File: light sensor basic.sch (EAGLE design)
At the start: 1 part

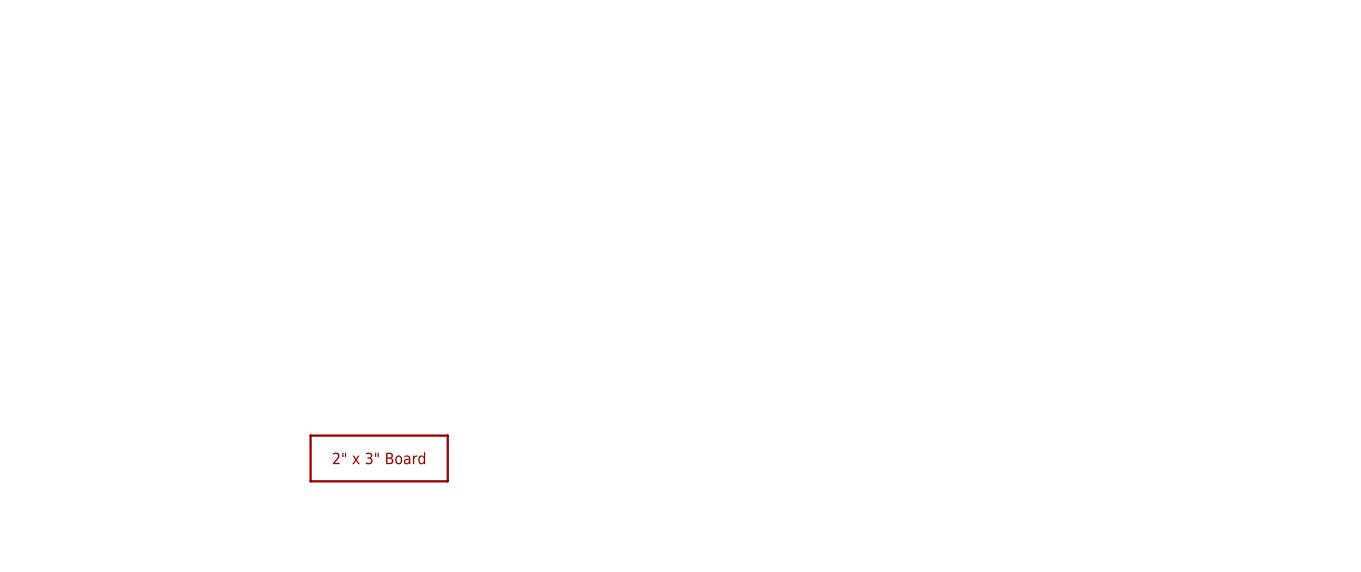
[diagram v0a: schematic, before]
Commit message: Update light sensor basic.sch
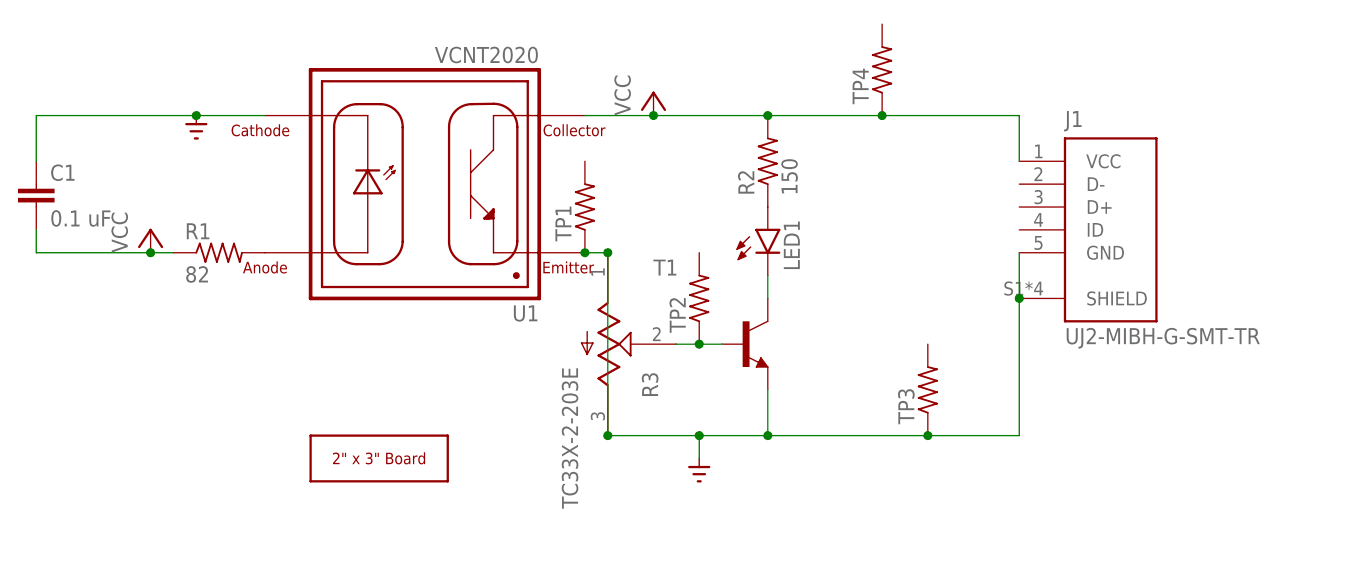
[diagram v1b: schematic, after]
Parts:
- added C1: 0.1 uF, rcl:C-EUC1206
- added J1: UJ2-MIBH-G-SMT-TR, UJ2-MIBH-G-SMT-TR:UJ2-MIBH-G-SMT-TR
- added LED1: (no value), led:LEDSML0805
- added R1: 82, rcl:R-US_R0805
- added R2: 150, rcl:R-US_R0805
- added R3: TC33X-2-203E, TC33X-2-203E:TC33X-2-203E
- added T1: (no value), transistor:-NPN-SOT23-EBC
- added TP1, TP2, TP3, TP4: (no value), rcl:R-US_R1206
- added U1: VCNT2020, VCNT2020:VCNT2020
- U$1: value 2X3_BOARD_V2 -> 2X3_BOARD; device voltera_community_lib:2X3_BOARD_V2 -> voltera_community_lib:2X3_BOARD
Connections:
- new net GND: C1.1, J1.GND, J1.SHIELD, R3.CCW, R3.CW, T1.E, TP1.1, TP3.1, U1.CATHODE, U1.EMITTER
- new net N$1: R1.2, U1.ANODE
- new net N$2: J1.VCC, R2.2, TP4.1, U1.COLLECTOR
- new net N$4: R3.W, T1.B, TP2.1
- new net N$5: LED1.C, T1.C
- new net N$6: LED1.A, R2.1
- new net VCC: C1.2, R1.1

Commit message: Update board
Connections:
- removed net N$2: J1.VCC, R2.2, TP4.1, U1.COLLECTOR
- new net N$3: R3.CCW, TP1.1, U1.EMITTER
- net GND: no longer R3.CCW, TP1.1, U1.EMITTER
- net VCC: now also J1.VCC, R2.2, TP4.1, U1.COLLECTOR
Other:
- moved on the sheet: TP1
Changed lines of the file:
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@@
 <instance part="U1" gate="VCNT2020" x="30.48" y="55.88" smashed="yes" rot="R180">
 <attribute name="NAME" x="43.18" y="42.418" size="1.778" layer="95" rot="R180"/>
-<attribute name="VALUE" x="43.18" y="71.12" size="1.778" layer="96" rot="R180"/>
 </instance>
 <instance part="GND1" gate="1" x="5.08" y="60.96" smashed="yes"/>
@@
 <instance part="C1" gate="G$1" x="-12.7" y="55.88" smashed="yes">
 <attribute name="NAME" x="-11.176" y="56.261" size="1.778" layer="95"/>
-<attribute name="VALUE" x="-11.176" y="51.181" size="1.778" layer="96"/>
 </instance>
-<instance part="P+2" gate="VCC" x="55.88" y="66.04" smashed="yes">
-<attribute name="VALUE" x="53.34" y="63.5" size="1.778" layer="96" rot="R90"/>
+<instance part="P+2" gate="VCC" x="55.88" y="71.12" smashed="yes">
+<attribute name="VALUE" x="53.34" y="68.58" size="1.778" layer="96" rot="R90"/>
 </instance>
 <instance part="R2" gate="G$1" x="68.58" y="58.42" smashed="yes" rot="R90">
@@
 <instance part="R3" gate="G$1" x="50.8" y="38.1" smashed="yes" rot="R270">
 <attribute name="NAME" x="54.613940625" y="35.04885" size="1.779840625" layer="95" rot="R270"/>
-<attribute name="VALUE" x="45.71583125" y="35.55791875" size="1.779459375" layer="96" rot="R270"/>
 </instance>
 <instance part="GND2" gate="1" x="60.96" y="22.86" smashed="yes"/>
@@
 <instance part="J1" gate="G$1" x="106.68" y="50.8" smashed="yes">
 <attribute name="NAME" x="101.6" y="62.23" size="1.778" layer="95"/>
-<attribute name="VALUE" x="101.6" y="38.1" size="1.778" layer="96"/>
 </instance>
-<instance part="TP1" gate="G$1" x="48.26" y="53.34" smashed="yes" rot="R90">
-<attribute name="NAME" x="46.7614" y="49.53" size="1.778" layer="95" rot="R90"/>
-<attribute name="VALUE" x="51.562" y="49.53" size="1.778" layer="96" rot="R90"/>
+<instance part="TP1" gate="G$1" x="45.72" y="53.34" smashed="yes" rot="R90">
+<attribute name="NAME" x="44.2214" y="49.53" size="1.778" layer="95" rot="R90"/>
+<attribute name="VALUE" x="49.022" y="49.53" size="1.778" layer="96" rot="R90"/>
 </instance>
 <instance part="TP2" gate="G$1" x="60.96" y="43.18" smashed="yes" rot="R90">
@@
 </instance>
 <instance part="TP4" gate="G$1" x="81.28" y="68.58" smashed="yes" rot="R90">
-<attribute name="NAME" x="79.7814" y="64.77" size="1.778" layer="95" rot="R90"/>
 <attribute name="VALUE" x="84.582" y="64.77" size="1.778" layer="96" rot="R90"/>
 </instance>
@@
 </segment>
 <segment>
-<pinref part="U1" gate="VCNT2020" pin="EMITTER"/>
 <pinref part="R3" gate="G$1" pin="CW"/>
-<wire x1="48.26" y1="48.26" x2="50.8" y2="48.26" width="0.1524" layer="91"/>
-<pinref part="R3" gate="G$1" pin="CCW"/>
-<wire x1="50.8" y1="48.26" x2="50.8" y2="27.94" width="0.1524" layer="91"/>
-<junction x="50.8" y="48.26"/>
 <wire x1="50.8" y1="27.94" x2="60.96" y2="27.94" width="0.1524" layer="91"/>
-<junction x="50.8" y="27.94"/>
 <pinref part="T1" gate="G$1" pin="E"/>
 <wire x1="60.96" y1="27.94" x2="68.58" y2="27.94" width="0.1524" layer="91"/>
@@
 <junction x="96.52" y="43.18"/>
 <junction x="68.58" y="27.94"/>
-<pinref part="TP1" gate="G$1" pin="1"/>
-<junction x="48.26" y="48.26"/>
 <pinref part="TP3" gate="G$1" pin="1"/>
 <wire x1="86.36" y1="27.94" x2="68.58" y2="27.94" width="0.1524" layer="91"/>
@@
 <junction x="0" y="48.26"/>
 </segment>
-</net>
-<net name="N$2" class="0">
 <segment>
-<pinref part="U1" gate="VCNT2020" pin="COLLECTOR"/>
 <pinref part="R2" gate="G$1" pin="2"/>
-<wire x1="48.26" y1="63.5" x2="55.88" y2="63.5" width="0.1524" layer="91"/>
-<pinref part="P+2" gate="VCC" pin="VCC"/>
-<wire x1="55.88" y1="63.5" x2="68.58" y2="63.5" width="0.1524" layer="91"/>
-<junction x="55.88" y="63.5"/>
 <pinref part="J1" gate="G$1" pin="VCC"/>
 <wire x1="96.52" y1="58.42" x2="96.52" y2="63.5" width="0.1524" layer="91"/>
 <wire x1="96.52" y1="63.5" x2="81.28" y2="63.5" width="0.1524" layer="91"/>
-<junction x="68.58" y="63.5"/>
 <pinref part="TP4" gate="G$1" pin="1"/>
 <wire x1="81.28" y1="63.5" x2="68.58" y2="63.5" width="0.1524" layer="91"/>
 <junction x="81.28" y="63.5"/>
+<pinref part="U1" gate="VCNT2020" pin="COLLECTOR"/>
+<wire x1="48.26" y1="63.5" x2="55.88" y2="63.5" width="0.1524" layer="91"/>
+<junction x="68.58" y="63.5"/>
+<pinref part="P+2" gate="VCC" pin="VCC"/>
+<wire x1="55.88" y1="63.5" x2="68.58" y2="63.5" width="0.1524" layer="91"/>
+<wire x1="55.88" y1="68.58" x2="55.88" y2="63.5" width="0.1524" layer="91"/>
+<junction x="55.88" y="63.5"/>
 </segment>
 </net>
@@
 </segment>
 </net>
+<net name="N$3" class="0">
+<segment>
+<pinref part="U1" gate="VCNT2020" pin="EMITTER"/>
+<pinref part="R3" gate="G$1" pin="CCW"/>
+<wire x1="45.72" y1="48.26" x2="50.8" y2="48.26" width="0.1524" layer="91"/>
+<pinref part="TP1" gate="G$1" pin="1"/>
+<junction x="45.72" y="48.26"/>
+<wire x1="45.72" y1="48.26" x2="48.26" y2="48.26" width="0.1524" layer="91"/>
+</segment>
+</net>
